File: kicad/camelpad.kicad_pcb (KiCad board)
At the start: 2 copper layers, 90 x 75 mm, 33 parts, among them J1 USB_C_Receptacle_USB2.0_16P, J3 Molex PicoBlade 533980471, SW1 SWITCH_PUSHBUTTON_KAILH_SOCKET, SW2 SWITCH_PUSHBUTTON_KAILH_SOCKET, SW3 SWITCH_PUSHBUTTON_KAILH_SOCKET, SW4 SWITCH_PUSHBUTTON_KAILH_SOCKET, SW5 SWITCH_PUSHBUTTON_KAILH_SOCKET, SW6 SWITCH_PUSHBUTTON_KAILH_SOCKET, U1 ATtiny816-M, U2 AP2127K-3.3

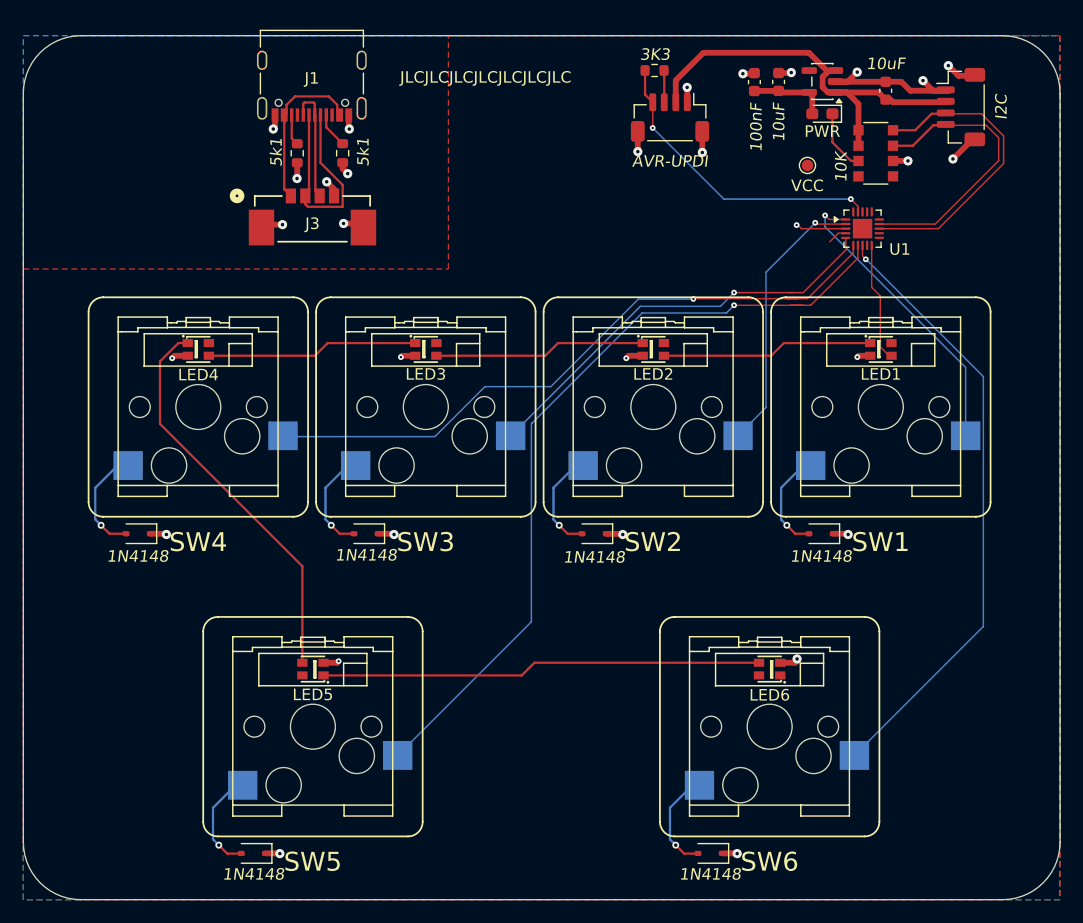
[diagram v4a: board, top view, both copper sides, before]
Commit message: Remove LDO as it's not needed. Clean 3v3 power comes from the controller
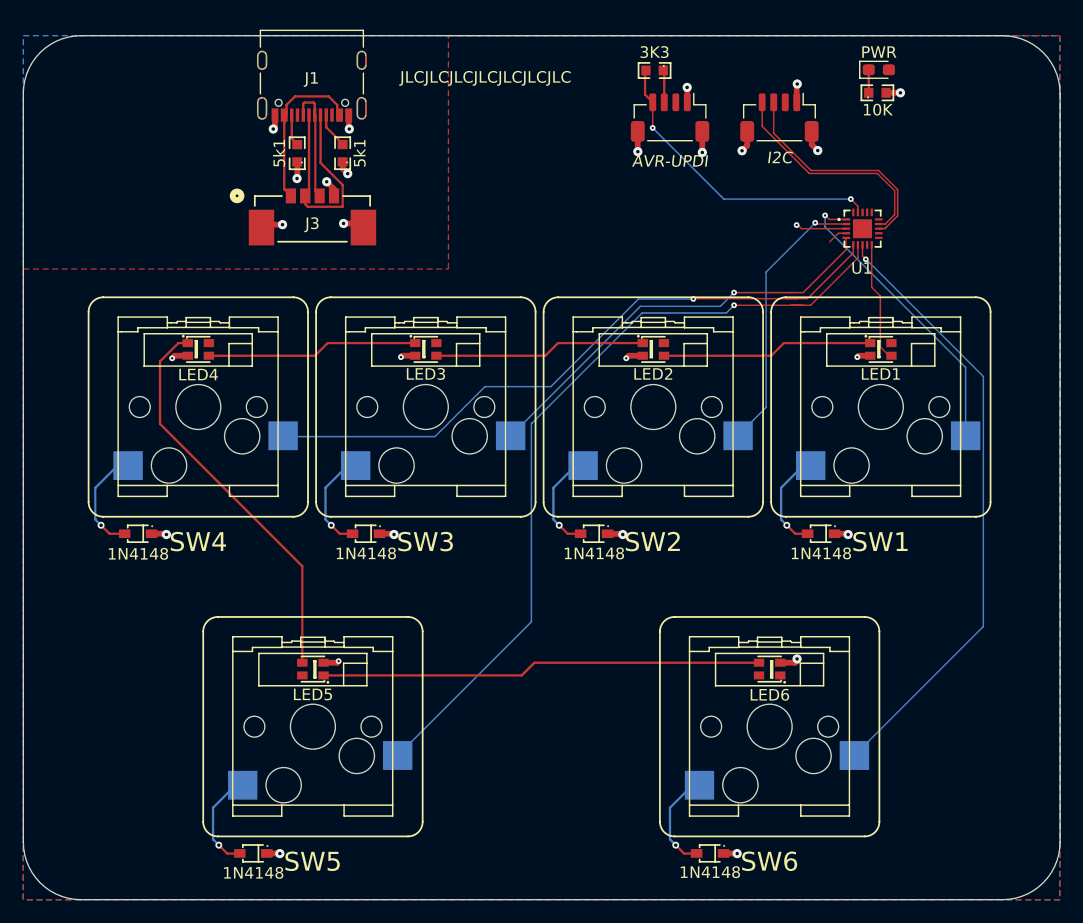
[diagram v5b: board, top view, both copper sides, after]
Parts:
- removed C1, C2: 10uF, camelpad:C_0603_1608Metric
- removed C3: 100nF, camelpad:C_0603_1608Metric
- removed RN1: 10K, camelpad:R_Array_Convex_4x1206
- removed U2: AP2127K-3.3, Package_TO_SOT_SMD:SOT-23-5
- removed VCC: TestPoint, TestPoint:TestPoint_Pad_D1.0mm
- added R4: 10K, camelpad:R0603, F.Cu at (124.1, 30.0)
- D1, D2, D3, D4, D5, D6: footprint camelpad:D_SOD-323 -> camelpad:SOD-323_L1.8-W1.3-LS2.5-RD
- R1, R2, R3: footprint camelpad:R_0603_1608Metric -> camelpad:R0603
- U1: value ATtiny816-M -> ATtiny1616-M; footprint camelpad:VQFN-20-1EP_3x3mm_P0.4mm_EP1.7x1.7mm -> camelpad:QFN-20_L3.0-W3.0-P0.40-BL-EP1.7
- moved I2C1 15.8 mm to (115.6, 32.1), turned to 180 degrees
- moved D7 6.21 mm to (124.3, 28.0), turned to 0 degrees
- turned U1 to -90 degrees
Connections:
- I2C1 pad 2: VIN -> VCC
- UPDI1 pad 2: VIN -> VCC
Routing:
- net VIN: track 36.7 -> 0.00 mm
- net GND: track 60.2 -> 42.5 mm, vias 30 -> 27
- net /SDA: track 26.5 -> 19.9 mm
- net VCC: track 8.28 -> 1.71 mm
- net /SCL: track 25.0 -> 19.7 mm
- net Net-(D7-K): track 5.41 -> 2.00 mm
